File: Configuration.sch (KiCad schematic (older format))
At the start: 13 parts, among them CON1 AVR-JTAG-10, Q1 IRLML2502, Q2 IRLML2502, U1 xc7a50tftg256

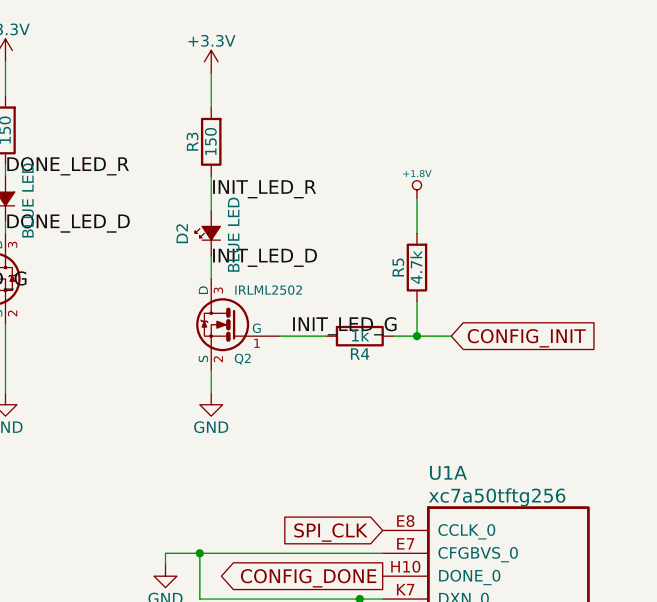
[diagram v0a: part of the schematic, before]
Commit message: encoders and headphone jack have been modified. many unconnections
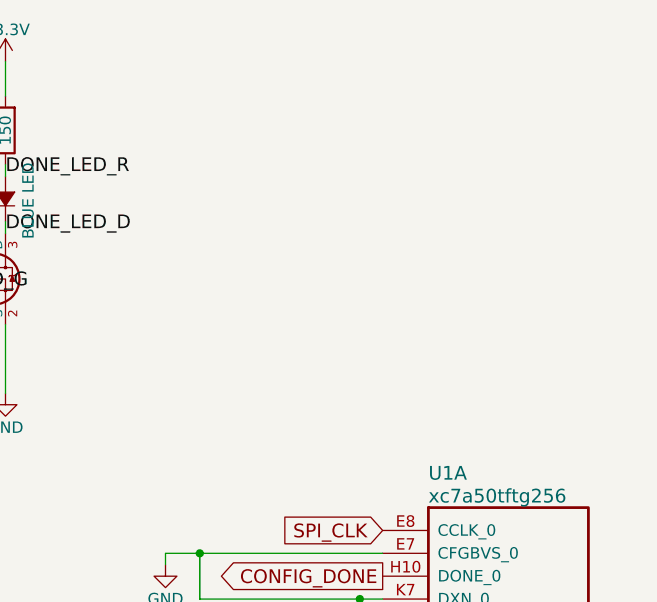
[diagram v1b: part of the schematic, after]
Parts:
- removed D2: BLUE LED, LEDs:LED_0603, symbol Led_Small
- removed Q2: IRLML2502, TO_SOT_Packages_SMD:SOT-23, symbol IRLML2502
- removed R3: 150, Resistors_SMD:R_0402, symbol R
- removed R4: 1k, Resistors_SMD:R_0402, symbol R
- removed R5: 4.7k, Resistors_SMD:R_0402, symbol R
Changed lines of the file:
@@
 LIBS:DFTCustom
 LIBS:TLV320AIC3104
+LIBS:tpa2010d1
+LIBS:lis2hh12
+LIBS:Ghost
+LIBS:asflmb
+LIBS:er-con06hb-1
+LIBS:jack_trs_4pins
 EELAYER 25 0
 EELAYER END
@@
 	1    0    0    -1
 $EndComp
-$Comp
-L R R5
-U 1 1 585C2C5F
-P 5450 1600
-F 0 "R5" V 5530 1600 50  0000 C CNN
-F 1 "4.7k" V 5450 1600 50  0000 C CNN
-F 2 "Resistors_SMD:R_0402" V 5380 1600 50  0001 C CNN
-F 3 "" H 5450 1600 50  0000 C CNN
-	1    5450 1600
-	-1   0    0    1
-$EndComp
 Text GLabel 5300 3350 0    60   Output ~ 0
 CONFIG_INIT
@@
 $EndComp
 $Comp
-L Led_Small D2
-U 1 1 585C498C
-P 4550 1450
-F 0 "D2" H 4500 1575 50  0000 L CNN
-F 1 "BLUE LED" H 4375 1350 50  0000 L CNN
-F 2 "LEDs:LED_0603" V 4550 1450 50  0001 C CNN
-F 3 "" V 4550 1450 50  0000 C CNN
-	1    4550 1450
-	0    -1   -1   0
-$EndComp
-$Comp
 L Led_Small D1
 U 1 1 585C4BD7
@@
 $EndComp
 $Comp
-L R R3
-U 1 1 585C4C4D
-P 4550 1050
-F 0 "R3" V 4630 1050 50  0000 C CNN
-F 1 "150" V 4550 1050 50  0000 C CNN
-F 2 "Resistors_SMD:R_0402" V 4480 1050 50  0001 C CNN
-F 3 "" H 4550 1050 50  0000 C CNN
-	1    4550 1050
-	-1   0    0    1
-$EndComp
-$Comp
 L C_Small C1
 U 1 1 586C7651
@@
 	0    1    1    0
 $EndComp
-$Comp
-L IRLML2502 Q2
-U 1 1 58759DB1
-P 4650 1850
-F 0 "Q2" H 4650 1701 40  0000 R CNN
-F 1 "IRLML2502" H 4650 2000 40  0000 R CNN
-F 2 "TO_SOT_Packages_SMD:SOT-23" H 4520 1952 29  0001 C CNN
-F 3 "" H 4650 1850 60  0000 C CNN
-	1    4650 1850
-	-1   0    0    -1
-$EndComp
-$Comp
-L R R4
-U 1 1 58759E3E
-P 5200 1900
-F 0 "R4" V 5280 1900 50  0000 C CNN
-F 1 "1k" V 5200 1900 50  0000 C CNN
-F 2 "Resistors_SMD:R_0402" V 5130 1900 50  0001 C CNN
-F 3 "" H 5200 1900 50  0000 C CNN
-	1    5200 1900
-	0    1    1    0
-$EndComp
 Wire Wire Line
 	3650 700  3650 850
@@
 Wire Wire Line
 	3650 1150 3650 1200
-Wire Wire Line
-	4550 1650 4550 1550
-Wire Wire Line
-	4550 1200 4550 1350
 $Comp
 L +3.3V #PWR07
@@
 	1    0    0    -1
 $EndComp
-Wire Wire Line
-	4550 2150 4550 2050
 Wire Wire Line
 	3650 1450 3650 1400
@@
 Text GLabel 2600 1700 0    60   Input ~ 0
 CONFIG_DONE
-Text GLabel 5600 1900 2    60   Input ~ 0
-CONFIG_INIT
-Wire Wire Line
-	5600 1900 5350 1900
-Wire Wire Line
-	5450 1750 5450 1900
-Connection ~ 5450 1900
-$Comp
-L +1.8V #PWR08
-U 1 1 587E84F9
-P 5450 1300
-F 0 "#PWR08" H 5450 1440 20  0001 C CNN
-F 1 "+1.8V" H 5450 1410 30  0000 C CNN
-F 2 "" H 5450 1300 60  0001 C CNN
-F 3 "" H 5450 1300 60  0001 C CNN
-	1    5450 1300
-	1    0    0    -1
-$EndComp
-Wire Wire Line
-	5450 1300 5450 1450
 Wire Wire Line
 	4350 3450 5300 3450
@@
 	5050 4850 5300 4850
 Wire Wire Line
-	4550 750  4550 900
-$Comp
-L +3.3V #PWR010
-U 1 1 587E9CAF
-P 4550 750
-F 0 "#PWR010" H 4550 600 50  0001 C CNN
-F 1 "+3.3V" H 4550 890 50  0000 C CNN
-F 2 "" H 4550 750 50  0000 C CNN
-F 3 "" H 4550 750 50  0000 C CNN
-	1    4550 750
-	1    0    0    -1
-$EndComp
-$Comp
-L GND #PWR011
-U 1 1 587E9EC7
-P 4550 2150
-F 0 "#PWR011" H 4550 1900 50  0001 C CNN
-F 1 "GND" H 4550 2000 50  0000 C CNN
-F 2 "" H 4550 2150 50  0000 C CNN
-F 3 "" H 4550 2150 50  0000 C CNN
-	1    4550 2150
-	1    0    0    -1
-$EndComp
-Text Label 4550 1300 0    60   ~ 0
-INIT_LED_R
-Text Label 4550 1600 0    60   ~ 0
-INIT_LED_D
-Wire Wire Line
-	4850 1900 5050 1900
-Text Label 4900 1900 0    60   ~ 0
-INIT_LED_G
-Wire Wire Line
 	3350 1700 3100 1700

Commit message: using BOMs AWAY to create BOM
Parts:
- C1: MFR (none) -> Murata Manufacturing Co Ltd; MPN (none) -> GRM32ER70J476ME20L
- D1: MFR (none) -> Vishay Semiconductors; MPN (none) -> VLMB1300-GS08
- Q1: MFR (none) -> Infineon Technologies AG; MPN (none) -> IRLML2502TRPBF
- R1: MFR (none) -> Vishay Dale; MPN (none) -> CRCW04021K00FKED
- R2: MFR (none) -> Vishay Dale; MPN (none) -> CRCW0402150RFKED
- R77: MFR (none) -> Vishay Dale; MPN (none) -> CRCW04024K70FKED
- U1: MFR (none) -> Xilinx; MPN (none) -> XC7A50T-1FTG256C

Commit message: just added NOTE field to BOMS AWAY
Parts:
- C1: SPN (none) -> 490-6542-1-ND; SPR (none) -> Digikey
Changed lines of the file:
@@
 F 4 "Murata Manufacturing Co Ltd" H 0 0 50 0001 C CNN "MFR"
 F 5 "GRM32ER70J476ME20L" H 0 0 50 0001 C CNN "MPN"
-F 6 "" H 0 0 50 0001 C CNN "SPR"
-F 7 "" H 0 0 50 0001 C CNN "SPN"
+F 6 "Digikey" H 0 0 50 0001 C CNN "SPR"
+F 7 "490-6542-1-ND" H 0 0 50 0001 C CNN "SPN"
 F 8 "" H 0 0 50 0001 C CNN "SPURL"
 	1    4350 4400

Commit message: Complete BOM. all resistors now 0402
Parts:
- D1: SPN (none) -> VLMB1300-GS08CT-ND; SPR (none) -> Digikey
- Q1: SPN (none) -> IRLML2502PBFCT-ND; SPR (none) -> Digikey
- R1: MFR Vishay Dale -> Yageo; MPN CRCW04021K00FKED -> RC0402FR-071KL; SPN (none) -> 311-1.00KLRCT-ND; SPR (none) -> Digikey
- R2: MFR Vishay Dale -> Yageo; MPN CRCW0402150RFKED -> RC0402FR-07150RL; SPN (none) -> 311-150LRTR-ND; SPR (none) -> Digikey
- R77: MFR Vishay Dale -> Yageo; MPN CRCW04024K70FKED -> RC0402FR-074K7L; SPN (none) -> 311-4.7KLRCT-ND; SPR (none) -> Digikey
- U1: SPN (none) -> 122-1916-ND; SPR (none) -> Digikey

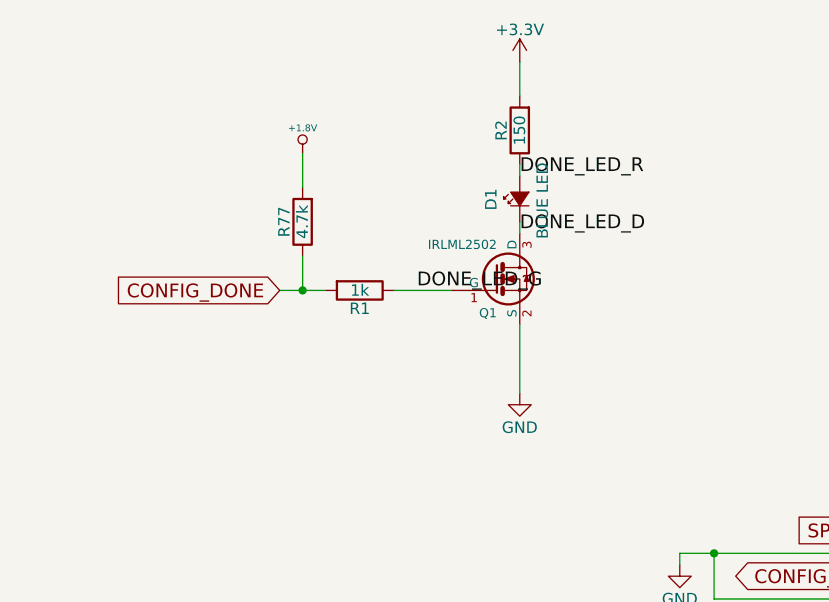
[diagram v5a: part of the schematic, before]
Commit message: added caps to audio
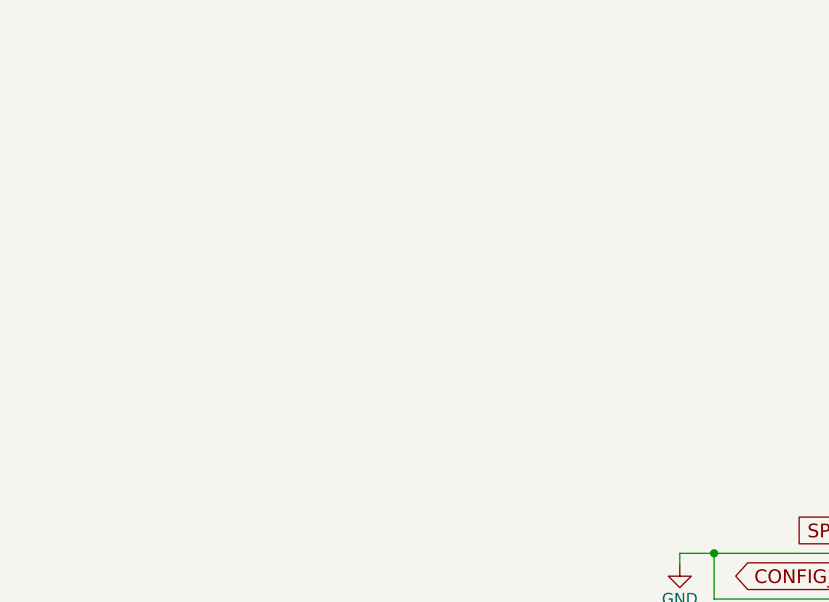
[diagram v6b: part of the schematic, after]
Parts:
- removed D1: BLUE LED, LEDs:LED_0603, symbol Led_Small
- removed Q1: IRLML2502, TO_SOT_Packages_SMD:SOT-23, symbol IRLML2502
- removed R1: 1k, Resistors_SMD:R_0402, symbol R
- removed R2: 150, Resistors_SMD:R_0402, symbol R
- removed R77: 4.7k, Resistors_SMD:R_0402, symbol R
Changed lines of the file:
@@
-$EndComp
-$Comp
-L Led_Small D1
-U 1 1 585C4BD7
-P 3650 1300
-F 0 "D1" H 3600 1425 50  0000 L CNN
-F 1 "BLUE LED" H 3475 1200 50  0000 L CNN
-F 2 "LEDs:LED_0603" V 3650 1300 50  0001 C CNN
-F 3 "" V 3650 1300 50  0001 C CNN
-F 4 "Vishay Semiconductors" H 0   0   50  0001 C CNN "MFR"
-F 5 "VLMB1300-GS08" H 0   0   50  0001 C CNN "MPN"
-F 6 "Digikey" H 0   0   50  0001 C CNN "SPR"
-F 7 "VLMB1300-GS08CT-ND" H 0   0   50  0001 C CNN "SPN"
-F 8 "" H 0   0   50  0001 C CNN "SPURL"
-	1    3650 1300
-	0    -1   -1   0
-$EndComp
-$Comp
-L R R2
-U 1 1 585C4C12
-P 3650 1000
-F 0 "R2" V 3730 1000 50  0000 C CNN
-F 1 "150" V 3650 1000 50  0000 C CNN
-F 2 "Resistors_SMD:R_0402" V 3580 1000 50  0001 C CNN
-F 3 "" H 3650 1000 50  0001 C CNN
-F 4 "Yageo" H 0   0   50  0001 C CNN "MFR"
-F 5 "RC0402FR-07150RL" H 0   0   50  0001 C CNN "MPN"
-F 6 "Digikey" H 0   0   50  0001 C CNN "SPR"
-F 7 "311-150LRTR-ND" H 0   0   50  0001 C CNN "SPN"
-F 8 "" H 0   0   50  0001 C CNN "SPURL"
-	1    3650 1000
-	-1   0    0    1
 $EndComp
 $Comp
@@
 $EndComp
 $Comp
-L IRLML2502 Q1
-U 1 1 58756D88
-P 3550 1650
-F 0 "Q1" H 3550 1501 40  0000 R CNN
-F 1 "IRLML2502" H 3550 1800 40  0000 R CNN
-F 2 "TO_SOT_Packages_SMD:SOT-23" H 3420 1752 29  0001 C CNN
-F 3 "" H 3550 1650 60  0001 C CNN
-F 4 "Infineon Technologies AG" H 0   0   50  0001 C CNN "MFR"
-F 5 "IRLML2502TRPBF" H 0   0   50  0001 C CNN "MPN"
-F 6 "Digikey" H 0   0   50  0001 C CNN "SPR"
-F 7 "IRLML2502PBFCT-ND" H 0   0   50  0001 C CNN "SPN"
-F 8 "" H 0   0   50  0001 C CNN "SPURL"
-	1    3550 1650
-	1    0    0    -1
-$EndComp
-$Comp
-L R R1
-U 1 1 58759D1F
-P 2950 1700
-F 0 "R1" V 3030 1700 50  0000 C CNN
-F 1 "1k" V 2950 1700 50  0000 C CNN
-F 2 "Resistors_SMD:R_0402" V 2880 1700 50  0001 C CNN
-F 3 "" H 2950 1700 50  0001 C CNN
-F 4 "Yageo" H 0   0   50  0001 C CNN "MFR"
-F 5 "RC0402FR-071KL" H 0   0   50  0001 C CNN "MPN"
-F 6 "Digikey" H 0   0   50  0001 C CNN "SPR"
-F 7 "311-1.00KLRCT-ND" H 0   0   50  0001 C CNN "SPN"
-F 8 "" H 0   0   50  0001 C CNN "SPURL"
-	1    2950 1700
-	0    1    1    0
-$EndComp
-$Comp
 L GND #PWR06
-U 1 1 5875AB8B
-P 3650 2150
-F 0 "#PWR06" H 3650 1900 50  0001 C CNN
-F 1 "GND" H 3650 2000 50  0000 C CNN
-F 2 "" H 3650 2150 50  0000 C CNN
-F 3 "" H 3650 2150 50  0000 C CNN
-	1    3650 2150
-	1    0    0    -1
-$EndComp
-$Comp
-L +3.3V #PWR07
-U 1 1 5876ED3D
-P 3650 700
-F 0 "#PWR07" H 3650 550 50  0001 C CNN
-F 1 "+3.3V" H 3650 840 50  0000 C CNN
-F 2 "" H 3650 700 50  0000 C CNN
-F 3 "" H 3650 700 50  0000 C CNN
-	1    3650 700
-	1    0    0    -1
-$EndComp
-$Comp
-L GND #PWR08
 U 1 1 587E913C
 P 4350 2900
-F 0 "#PWR08" H 4350 2650 50  0001 C CNN
+F 0 "#PWR06" H 4350 2650 50  0001 C CNN
 F 1 "GND" H 4350 2750 50  0000 C CNN
 F 2 "" H 4350 2900 50  0000 C CNN
 F 3 "" H 4350 2900 50  0000 C CNN
 	1    4350 2900
-	1    0    0    -1
-$EndComp
-$Comp
-L R R77
-U 1 1 5908E731
-P 2700 1400
-F 0 "R77" V 2780 1400 50  0000 C CNN
-F 1 "4.7k" V 2700 1400 50  0000 C CNN
-F 2 "Resistors_SMD:R_0402" V 2630 1400 50  0001 C CNN
-F 3 "" H 2700 1400 50  0001 C CNN
-F 4 "Yageo" H 0   0   50  0001 C CNN "MFR"
-F 5 "RC0402FR-074K7L" H 0   0   50  0001 C CNN "MPN"
-F 6 "Digikey" H 0   0   50  0001 C CNN "SPR"
-F 7 "311-4.7KLRCT-ND" H 0   0   50  0001 C CNN "SPN"
-F 8 "" H 0   0   50  0001 C CNN "SPURL"
-	1    2700 1400
-	-1   0    0    1
-$EndComp
-$Comp
-L +1.8V #PWR09
-U 1 1 5908E738
-P 2700 1100
-F 0 "#PWR09" H 2700 1240 20  0001 C CNN
-F 1 "+1.8V" H 2700 1210 30  0000 C CNN
-F 2 "" H 2700 1100 60  0001 C CNN
-F 3 "" H 2700 1100 60  0001 C CNN
-	1    2700 1100
 	1    0    0    -1
 $EndComp
@@
 Text GLabel 2600 4000 2    60   Output ~ 0
 AX_TMS
-Text GLabel 2600 1700 0    60   Input ~ 0
-CONFIG_DONE
-Text Label 3200 1700 0    60   ~ 0
-DONE_LED_G
-Text Label 3650 1200 0    60   ~ 0
-DONE_LED_R
-Text Label 3650 1450 0    60   ~ 0
-DONE_LED_D
 Wire Wire Line
 	4350 3550 5300 3550
@@
 	4350 4500 4350 4550
 Wire Wire Line
-	3650 700  3650 850
-Wire Wire Line
-	3650 1850 3650 2150
-Wire Wire Line
-	3650 1150 3650 1200
-Wire Wire Line
-	3650 1450 3650 1400
-Wire Wire Line
 	2600 3800 2250 3800
 Wire Wire Line
@@
 	5050 4850 5300 4850
 Wire Wire Line
-	3350 1700 3100 1700
-Wire Wire Line
 	5300 3150 5200 3150
 Wire Wire Line
@@
 Wire Wire Line
 	5200 3250 5300 3250
-Wire Wire Line
-	2700 1550 2700 1700
-Wire Wire Line
-	2700 1100 2700 1250
-Wire Wire Line
-	2600 1700 2800 1700
 Connection ~ 5200 4850
 Connection ~ 5200 4750
@@
 Connection ~ 4500 2850
 Connection ~ 5200 3150
-Connection ~ 2700 1700
 NoConn ~ 2000 4000
 NoConn ~ 2000 4100
